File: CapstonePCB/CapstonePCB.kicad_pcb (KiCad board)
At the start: 2 copper layers, 1 part, among them U1 NUCLEO64-F411RE

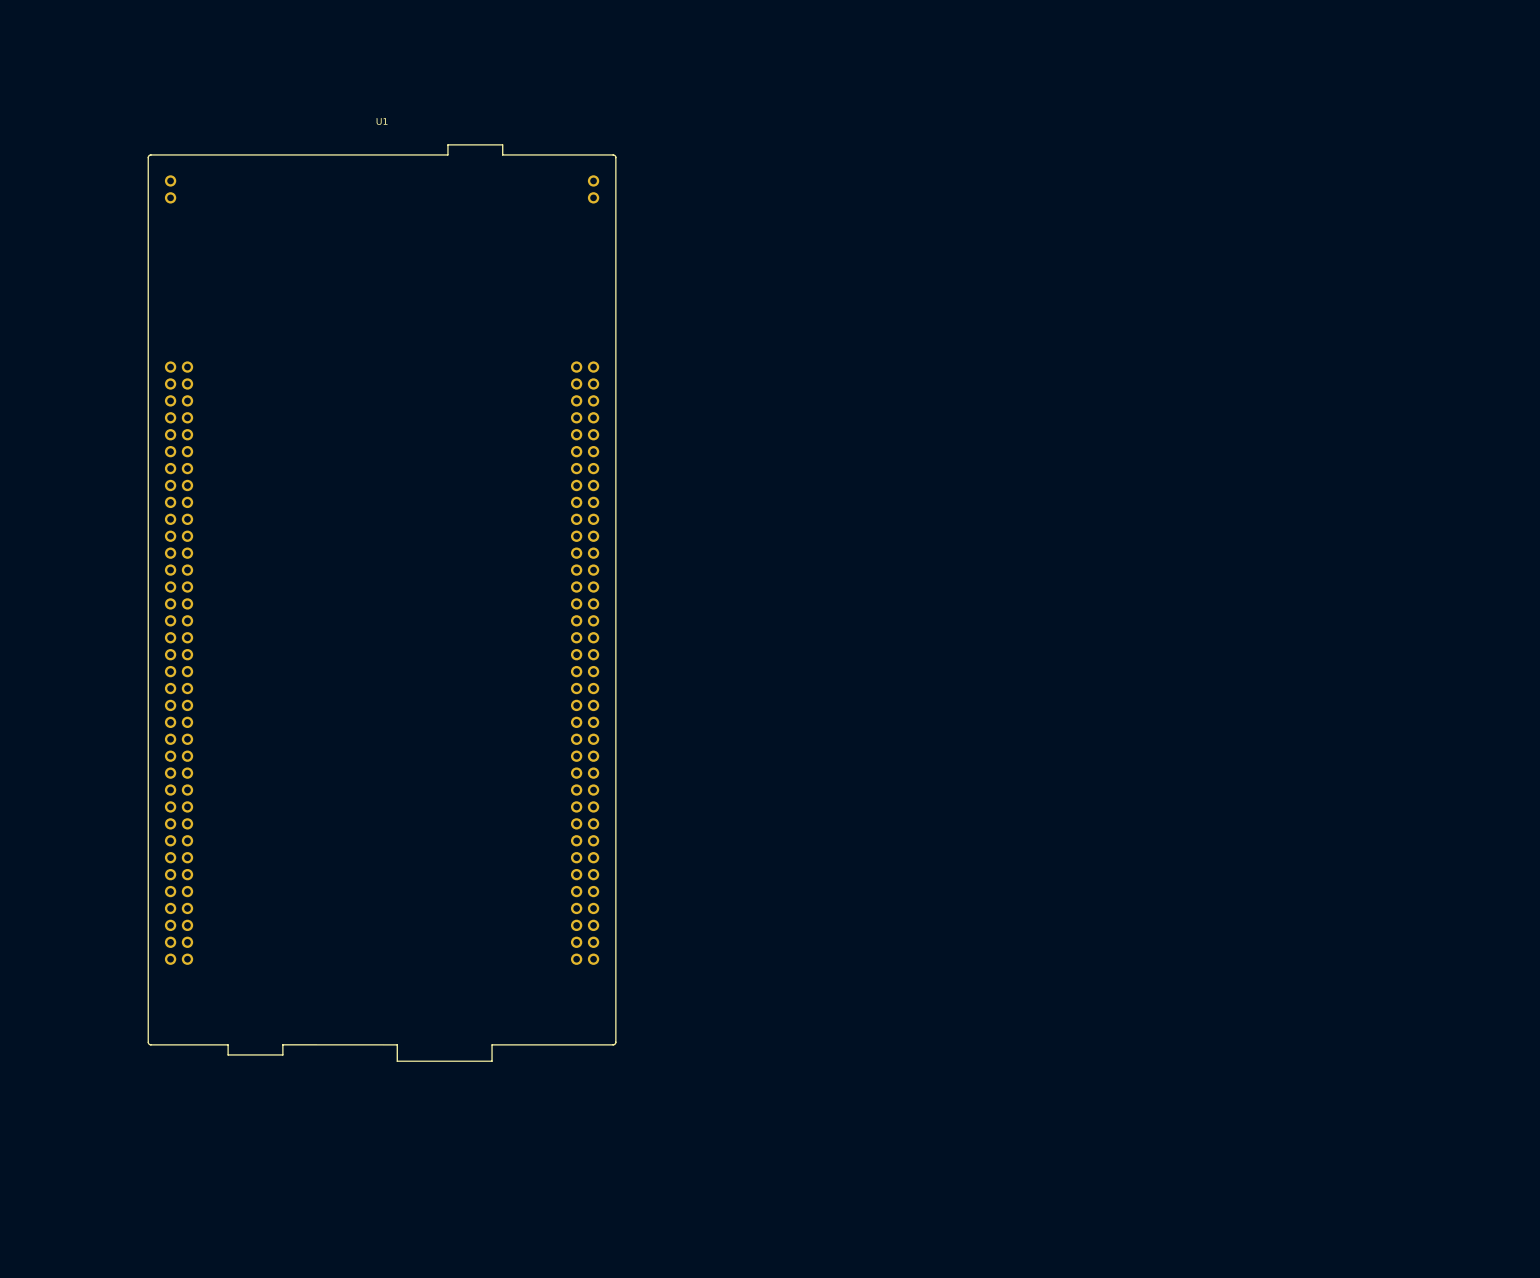
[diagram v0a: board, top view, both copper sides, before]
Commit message: Added MSPM0 outline to schematic.
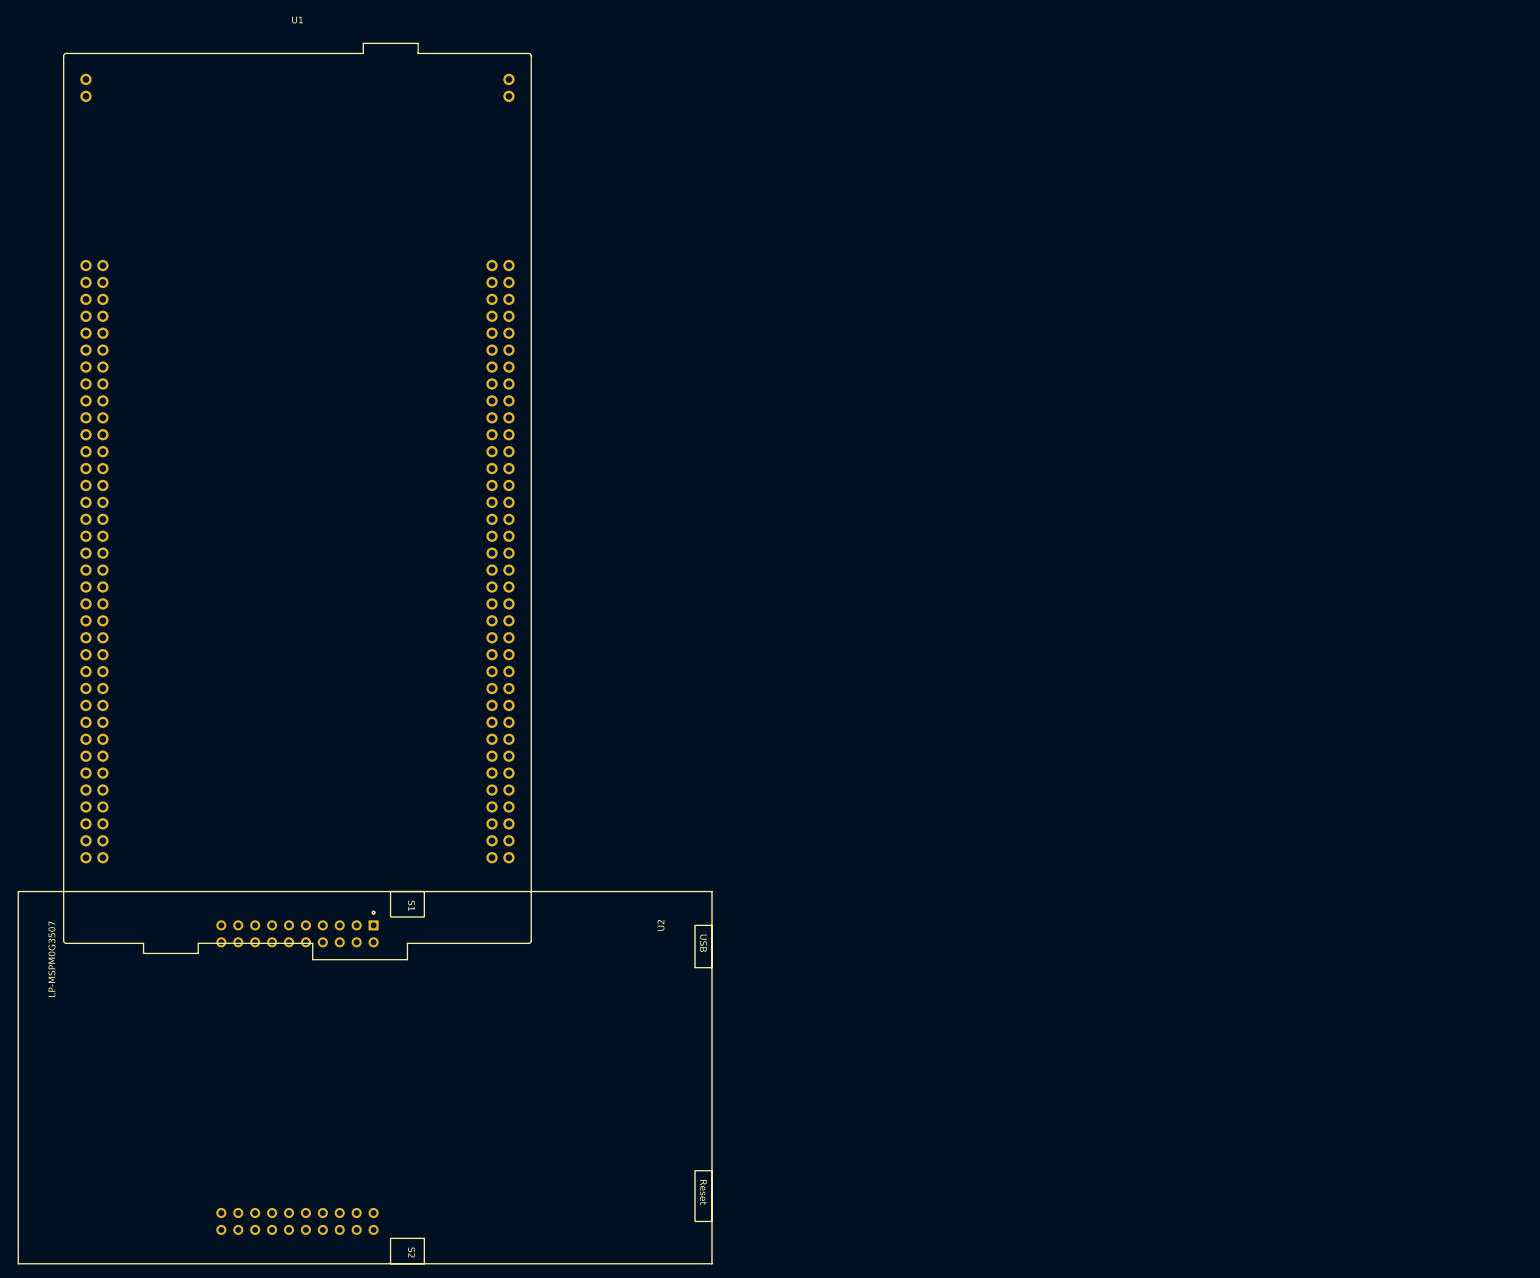
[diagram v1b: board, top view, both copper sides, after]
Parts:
- added U2: LP-MSPM0G3507, ECE319K:ti_LP_MSPM0G3507, F.Cu at (63.5, 167.6)
- moved U1 19.8 mm to (22.9, 45.7)

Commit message: Added a barrel jack for connection to wall power.
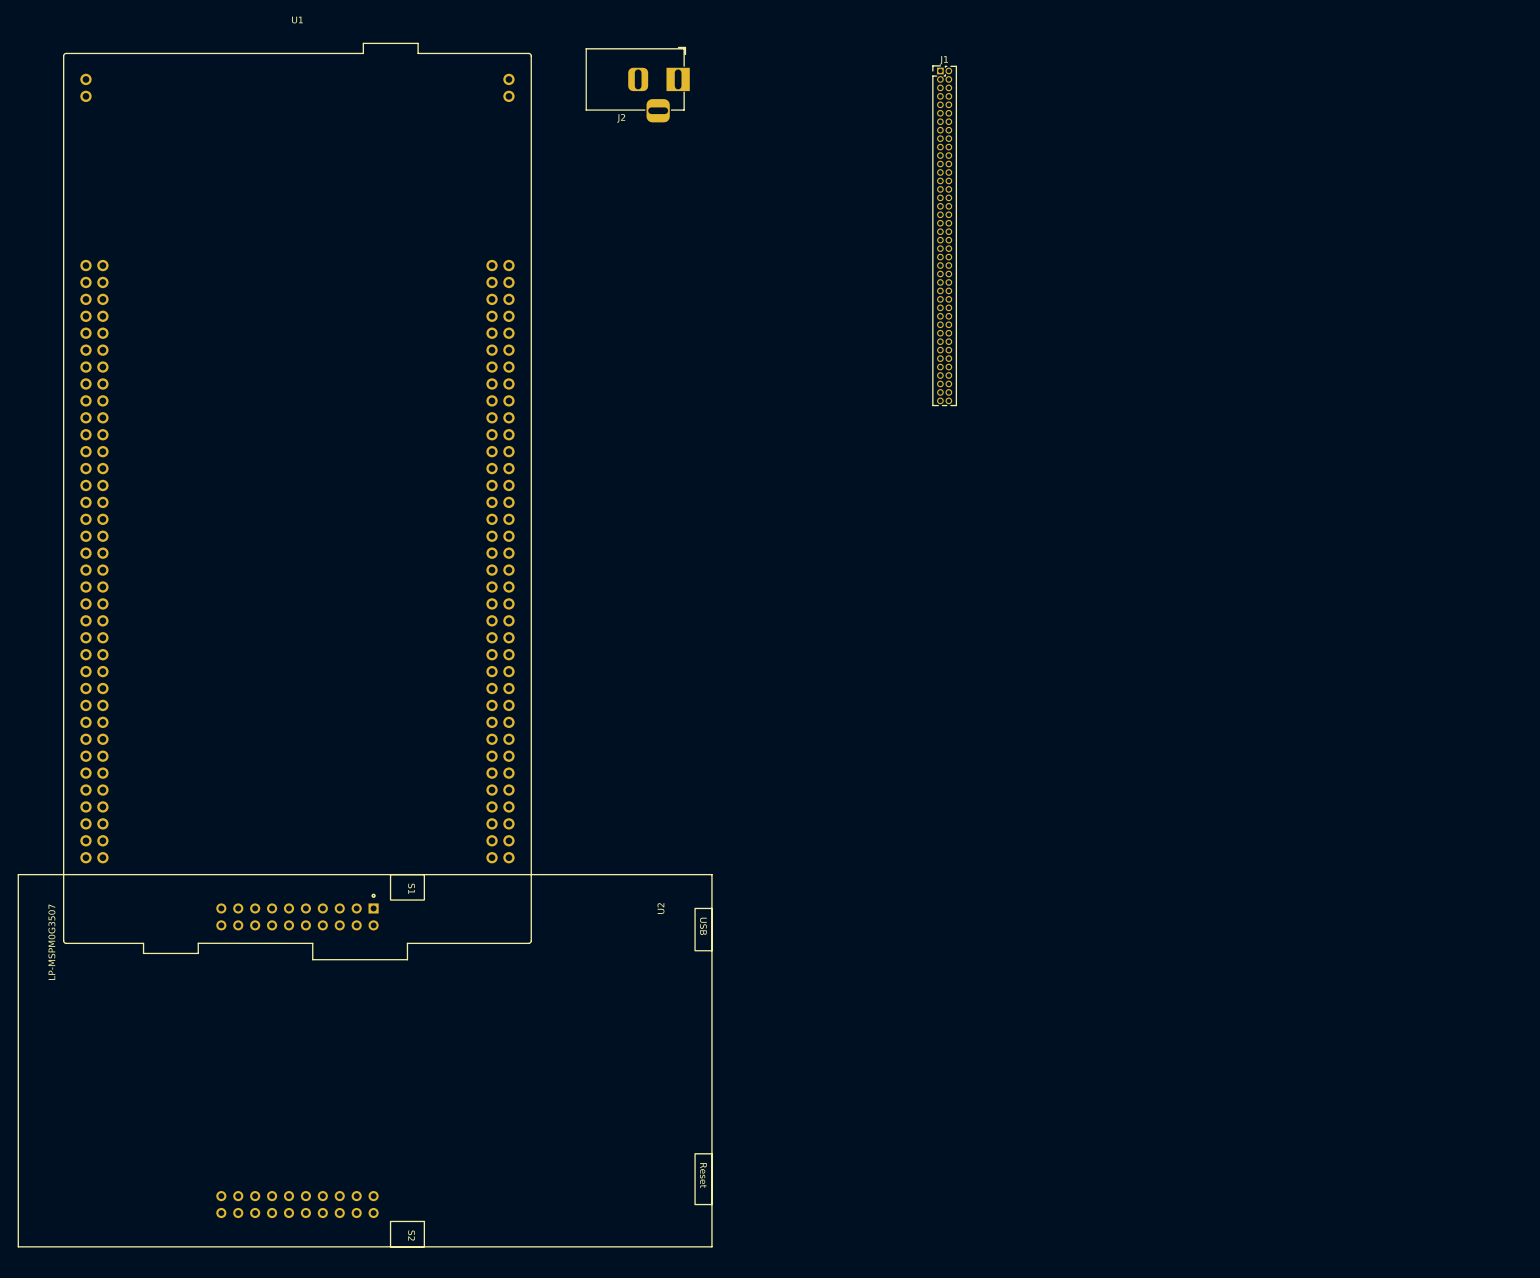
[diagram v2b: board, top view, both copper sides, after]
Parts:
- added J1: Conn_02x40_Counter_Clockwise, Connector_PinHeader_1.27mm:PinHeader_2x40_P1.27mm_Vertical, F.Cu at (151.1, 16.5)
- added J2: Barrel_Jack, Connector_BarrelJack:BarrelJack_Horizontal, F.Cu at (111.8, 17.8)
- moved U2 2.54 mm to (63.5, 165.1)

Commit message: Added barrel jack connector
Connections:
- J2 pad 2: unconnected-(J2-Pad2) -> GNDREF
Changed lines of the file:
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@@
   (net 200 "unconnected-(J1-Pin_80-Pad80)")
   (net 201 "unconnected-(J2-Pad1)")
-  (net 202 "unconnected-(J2-Pad2)")
+  (net 202 "GNDREF")
   (footprint "ECE319K:ti_LP_MSPM0G3507" (layer "F.Cu")
     (at 63.5 165.1 -90)
@@
       (net 201 "unconnected-(J2-Pad1)") (pintype "passive"))
     (pad "2" thru_hole roundrect (at -6 0) (size 3 3.5) (drill oval 1 3) (layers "*.Cu" "*.Mask") (roundrect_rratio 0.25)
-      (net 202 "unconnected-(J2-Pad2)") (pintype "passive"))
+      (net 202 "GNDREF") (pintype "passive"))
     (pad "3" thru_hole roundrect (at -3 4.7) (size 3.5 3.5) (drill oval 3 1) (layers "*.Cu" "*.Mask") (roundrect_rratio 0.25))
     (model "${KICAD6_3DMODEL_DIR}/Connector_BarrelJack.3dshapes/BarrelJack_Horizontal.wrl"

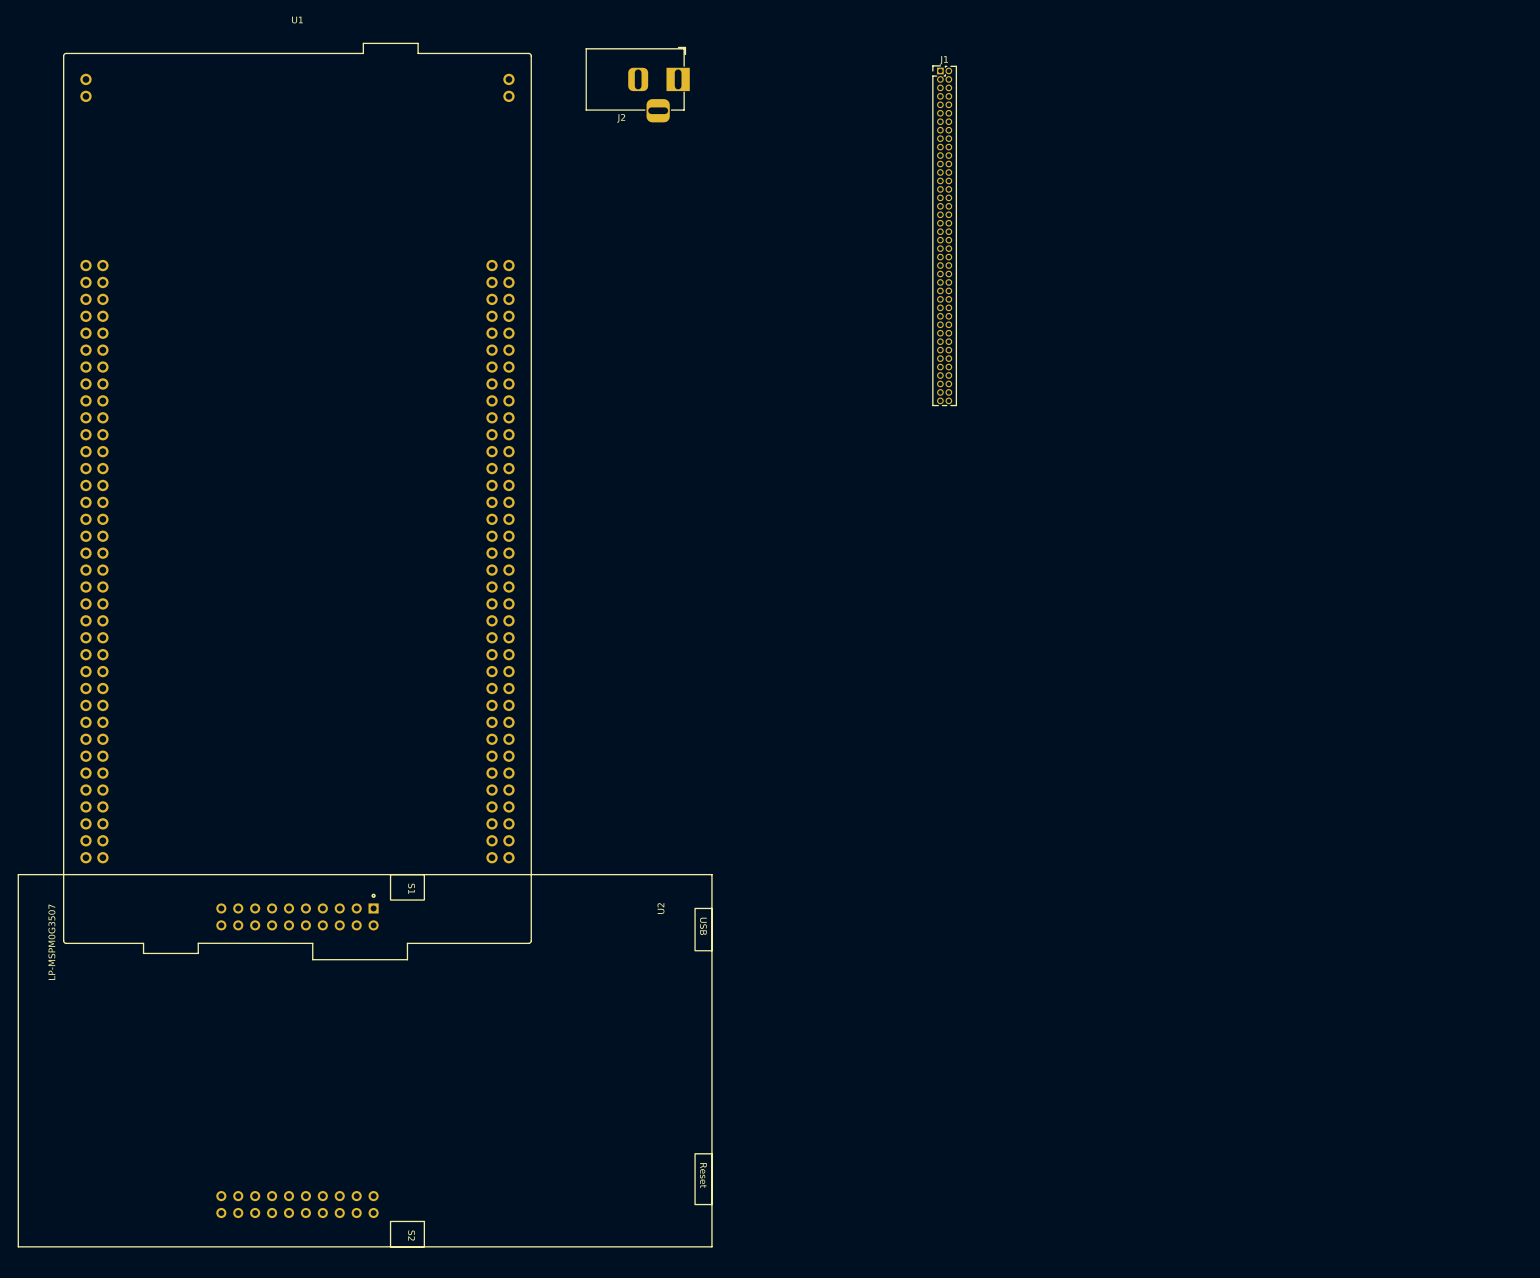
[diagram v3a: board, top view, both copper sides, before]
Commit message: Updated spacing for headers
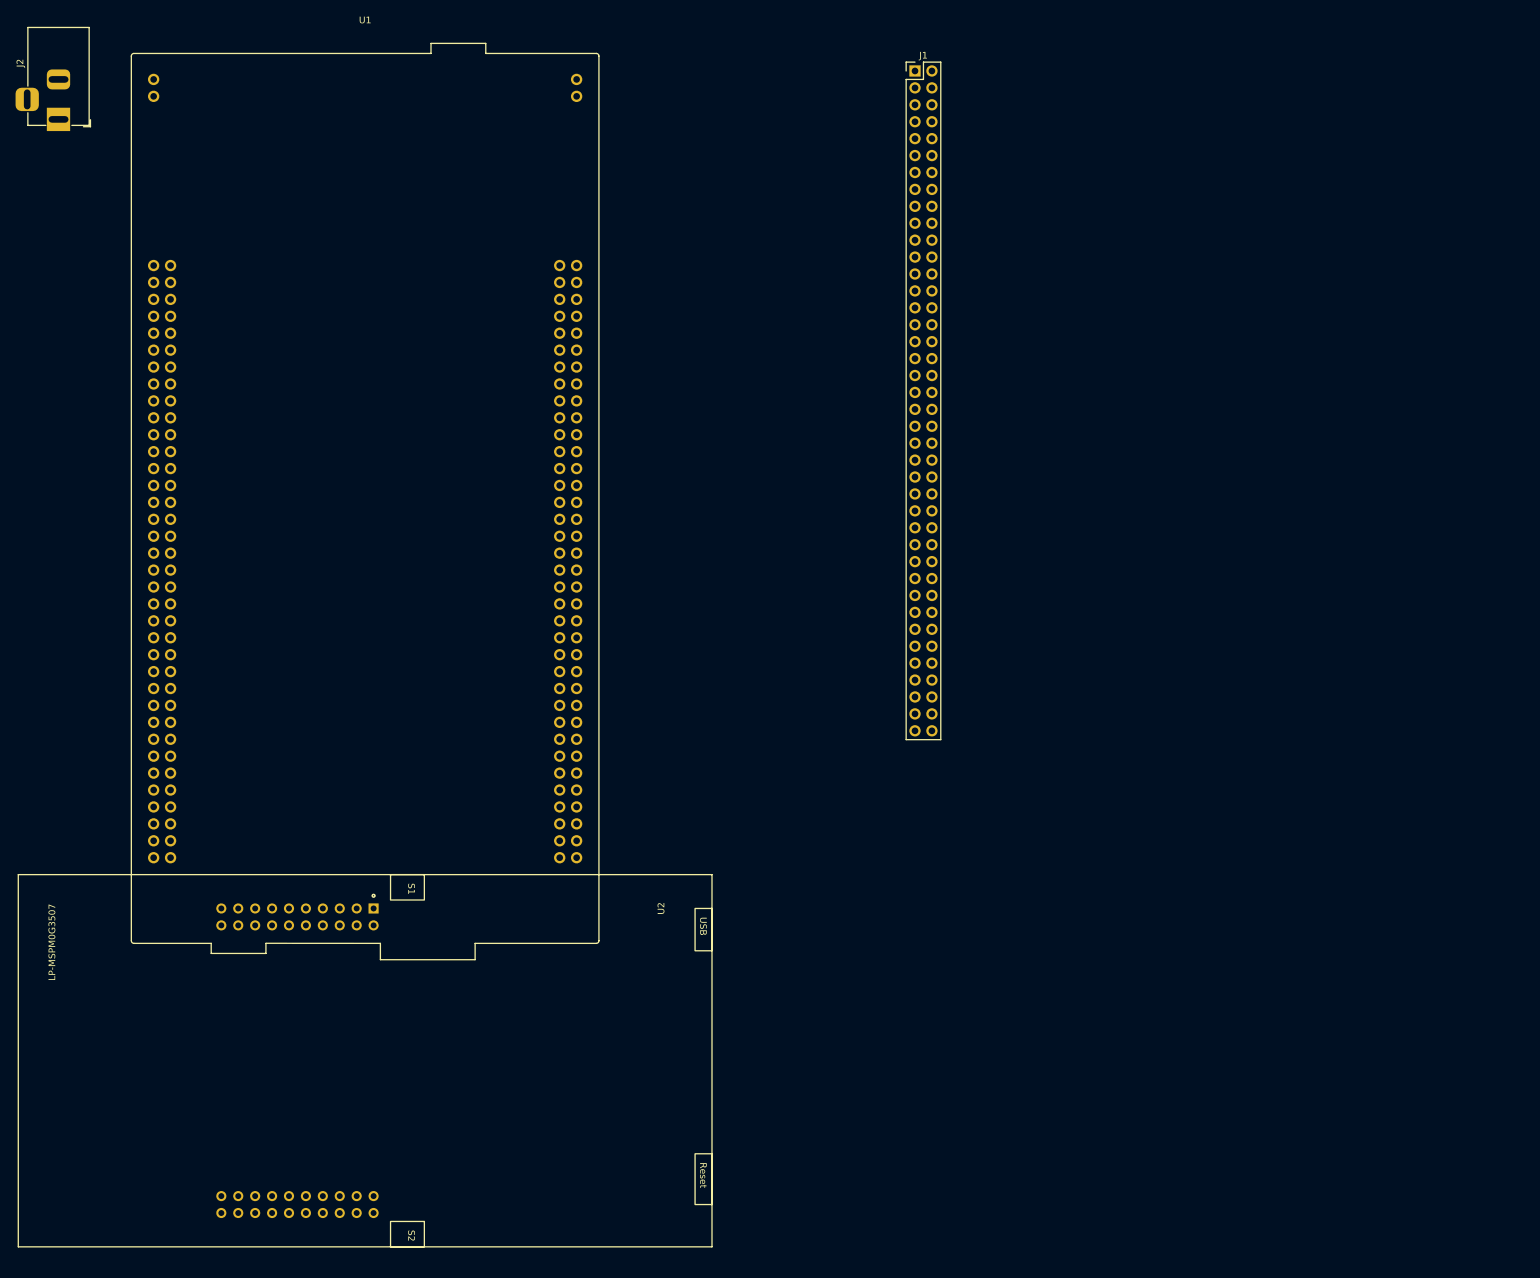
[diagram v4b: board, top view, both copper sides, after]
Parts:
- J1: footprint Connector_PinHeader_1.27mm:PinHeader_2x40_P1.27mm_Vertical -> Connector_PinHeader_2.54mm:PinHeader_2x40_P2.54mm_Vertical
- moved J2 93.2 mm to (18.7, 23.8), turned to -90 degrees
- moved U1 10.2 mm to (33.0, 45.7)
- moved J1 3.81 mm to (147.3, 16.5)

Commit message: Updated formating for stm32
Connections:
- J1 pad 1: unconnected-(J1-Pin_1-Pad1) -> Net-(J1-Pin_1)
- J1 pad 2: unconnected-(J1-Pin_2-Pad2) -> Net-(J1-Pin_2)
- J1 pad 3: unconnected-(J1-Pin_3-Pad3) -> Net-(J1-Pin_3)
- J1 pad 78: unconnected-(J1-Pin_78-Pad78) -> Net-(J1-Pin_3)
- J1 pad 79: unconnected-(J1-Pin_79-Pad79) -> Net-(J1-Pin_2)
- J1 pad 80: unconnected-(J1-Pin_80-Pad80) -> Net-(J1-Pin_1)
